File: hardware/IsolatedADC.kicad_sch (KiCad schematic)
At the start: 21 parts, among them IC3 OPA1679-Q1, IC4 ADS131M04, IC5 LTC1799, J6 CDMM20M0F2500DET, J9 CDMM20M0F2500DET

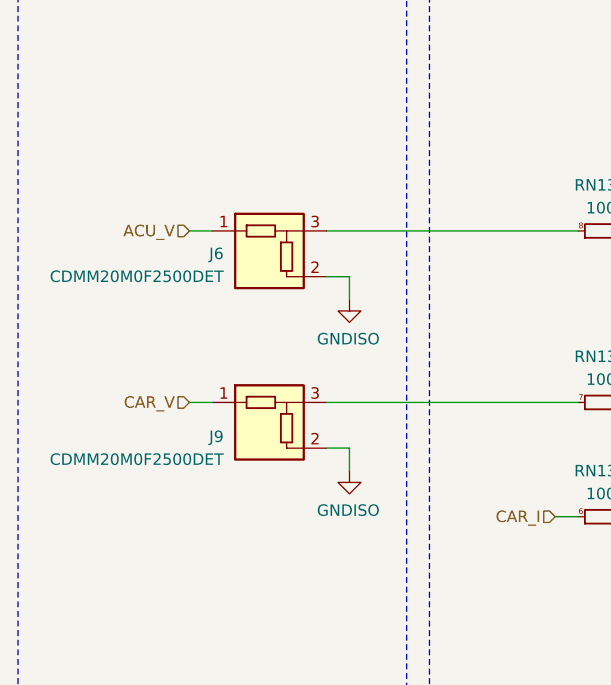
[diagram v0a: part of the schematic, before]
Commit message: new firmware for bga version of stm, change stm from smt to bga, smaller HV dividers, added 3rd can transciver, and other
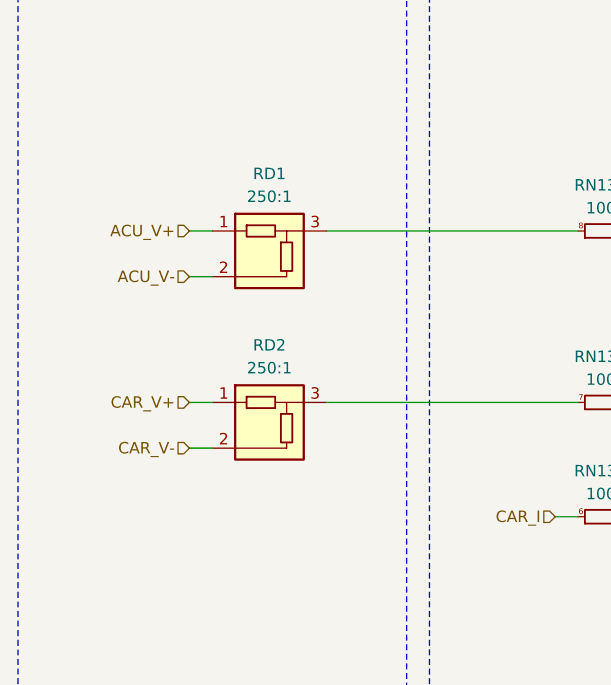
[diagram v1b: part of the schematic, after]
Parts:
- removed J6, J9: CDMM20M0F2500DET, Samacsys:CDMM20M0F2500DET, symbol Samacsys_kicad_sym:CDMM20M0F2500DET
- added RD1, RD2: 250:1, Samacsys:CDMA5M00F5000DE5, symbol Samacsys_kicad_sym:CDMA15M0D2500DE5
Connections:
- net at RN13.7 (R2.2): now also RD2.3
- net at RN13.8 (R1.2): now also RD1.3
- new net ACU_V+: RD1.1
- new net ACU_V-: RD1.2
- new net CAR_V+: RD2.1
- new net CAR_V-: RD2.2

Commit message: mama comit
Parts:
- removed C30: 10nF, Capacitor_SMD:C_0603_1608Metric, symbol Device:C_Small
- removed R1, R2, R3: 0, Resistor_SMD:R_0603_1608Metric, symbol Device:R_Small
- added R10: 10k, Resistor_SMD:R_0603_1608Metric, symbol Device:R_Small
- added R9: 100k, Resistor_SMD:R_0603_1608Metric, symbol Device:R_Small
- R15: value 10k -> 100k
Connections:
- net ACU_V- is gone; now on net GNDISO: RD1.2
- net CAR_V- is gone; now on net GNDISO: RD2.2
- net CAR_I_REF_ADC: no longer D4.1 (A), RN13.4 (R4.1)
- net GNDISO: now also R10.2
- net at IC3.11 (+): now also R10.1, R9.2
- new net: D4.1 (A), R9.1, RN13.4 (R4.1)
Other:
- moved on the sheet: D4, IC3A, IC3B, IC3C, IC3D, R15, R17, RD1, RD2, RN13A, RN13B, RN13C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

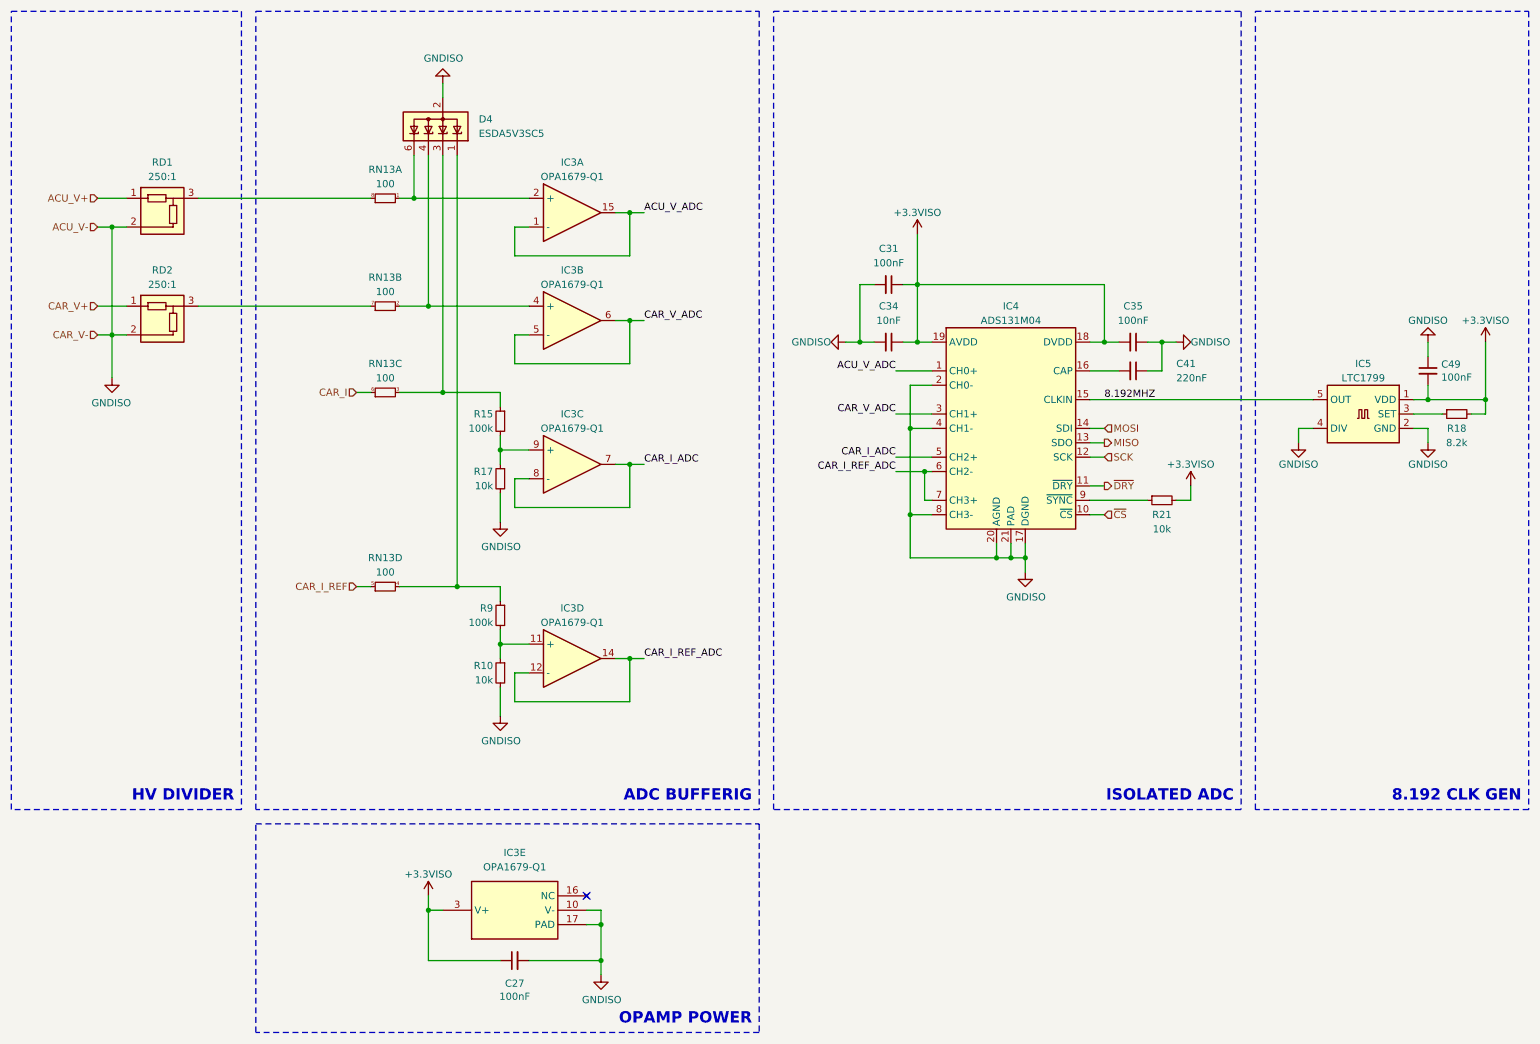
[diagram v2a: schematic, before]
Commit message: inductors 3d models fix, smaller relay (same series as the one from IMD), other + sync
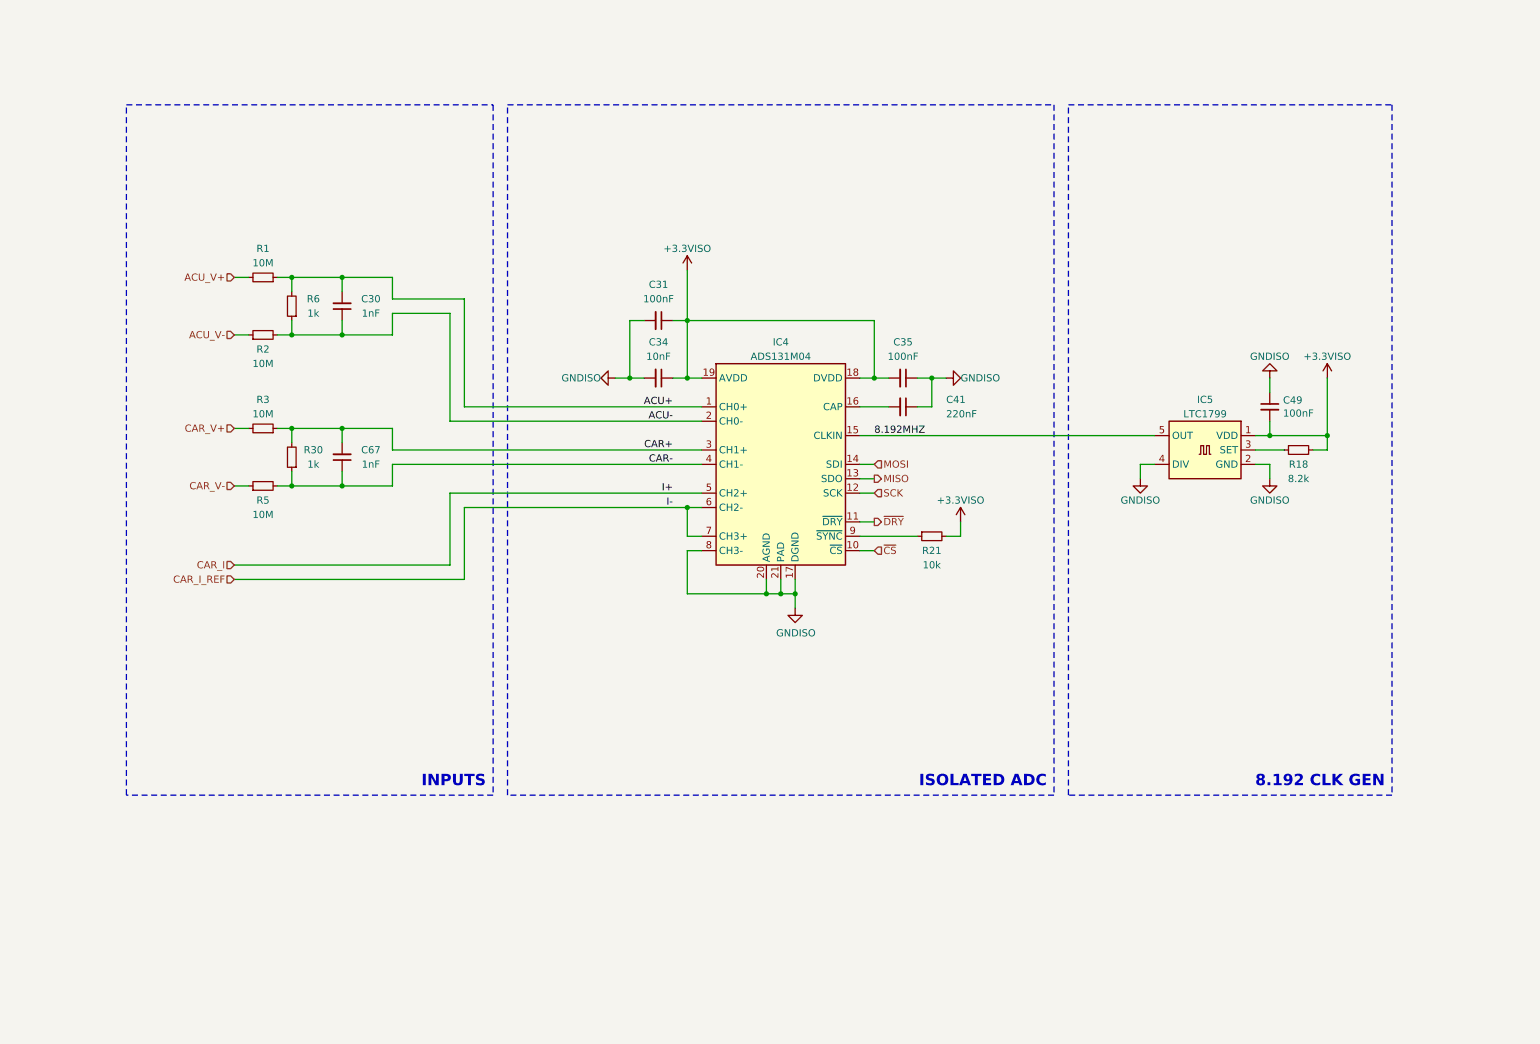
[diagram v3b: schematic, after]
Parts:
- removed C27: 100nF, Capacitor_SMD:C_0603_1608Metric, symbol Device:C_Small
- removed D4: ESDA5V3SC5, Package_TO_SOT_SMD:SOT-23-6, symbol Power_Protection:ESDA5V3SC5
- removed IC3: OPA1679-Q1, Package_DFN_QFN:QFN-16-1EP_4x4mm_P0.65mm_EP2.7x2.7mm, symbol Samacsys_kicad_sym:OPA1679-Q1
- removed R10, R17: 10k, Resistor_SMD:R_0603_1608Metric, symbol Device:R_Small
- removed R15, R9: 100k, Resistor_SMD:R_0603_1608Metric, symbol Device:R_Small
- removed RD1, RD2: 250:1, Samacsys:CDMA5M00F5000DE5, symbol Samacsys_kicad_sym:CDMA15M0D2500DE5
- removed RN13: 100, Resistor_SMD:R_Array_Convex_4x0603, symbol Device:R_Pack04_Split
- added C30, C67: 1nF, Capacitor_SMD:C_0603_1608Metric, symbol Device:C_Small
- added R1, R2, R3, R5: 10M, Resistor_SMD:R_0603_1608Metric, symbol Device:R_Small
- added R30, R6: 1k, Resistor_SMD:R_0603_1608Metric, symbol Device:R_Small
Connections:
- net CAR_I_ADC is gone; now on net CAR_I: IC4.5 (CH2+)
- net CAR_I_REF_ADC is gone; now on net CAR_I_REF: IC4.6 (CH2-), IC4.7 (CH3+)
- net ACU_V+: now also R1.2
- net CAR_V+: now also R3.2
- net GNDISO: no longer IC4.2 (CH0-), IC4.4 (CH1-)
- net ACU_V_ADC renamed ACU+
- net ACU+: now also C30.2, R1.1, R6.2
- net CAR_V_ADC renamed CAR+
- net CAR+: now also C67.2, R3.1, R30.2
- new net ACU-: C30.1, IC4.2 (CH0-), R2.2, R6.1
- new net ACU_V-: R2.1
- new net CAR-: C67.1, IC4.4 (CH1-), R30.1, R5.2
- new net CAR_V-: R5.1
- no-connect marks 1 -> 0
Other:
- note added: "INPUTS"
- note removed: "ADC BUFFERIG"
- note removed: "HV DIVIDER"
- note removed: "OPAMP POWER"
- moved on the sheet: C31, C34, C35, C41, C49, IC4, IC5, R18, R21

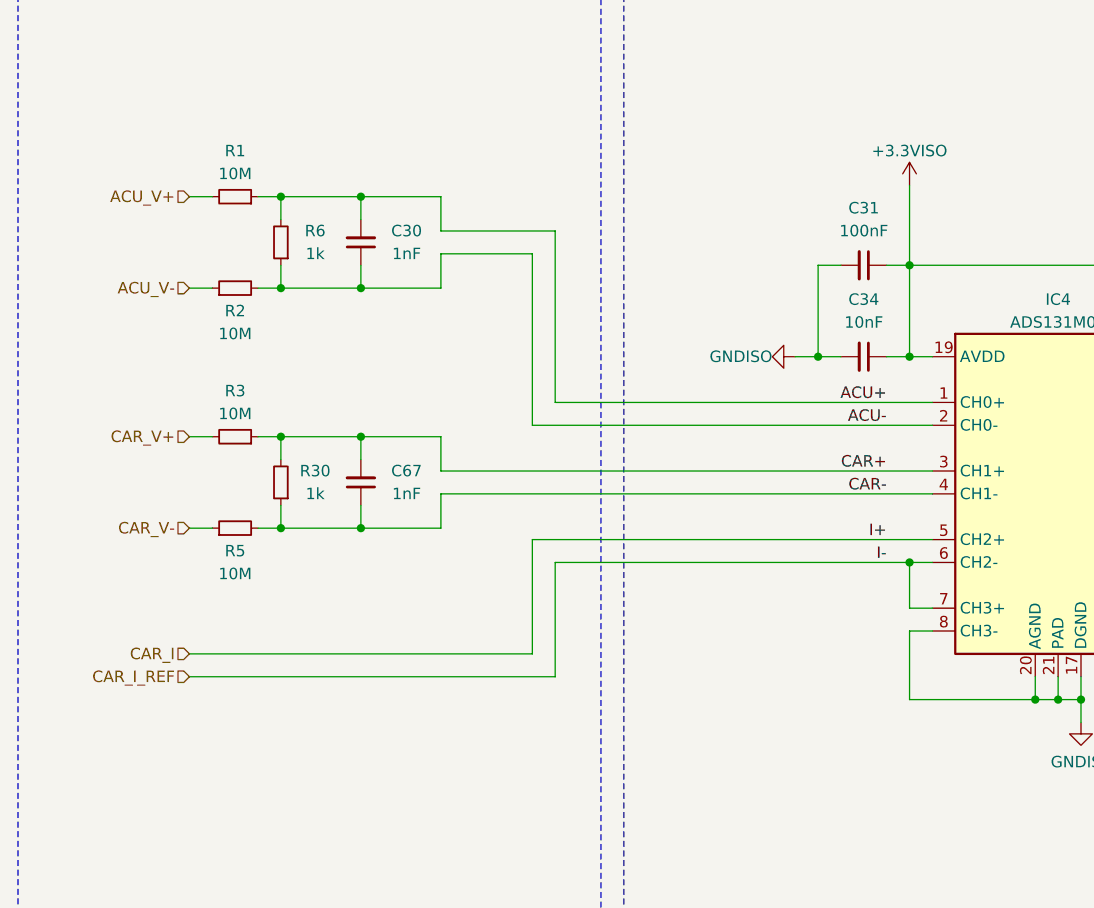
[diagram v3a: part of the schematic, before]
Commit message: all but the communications sections done
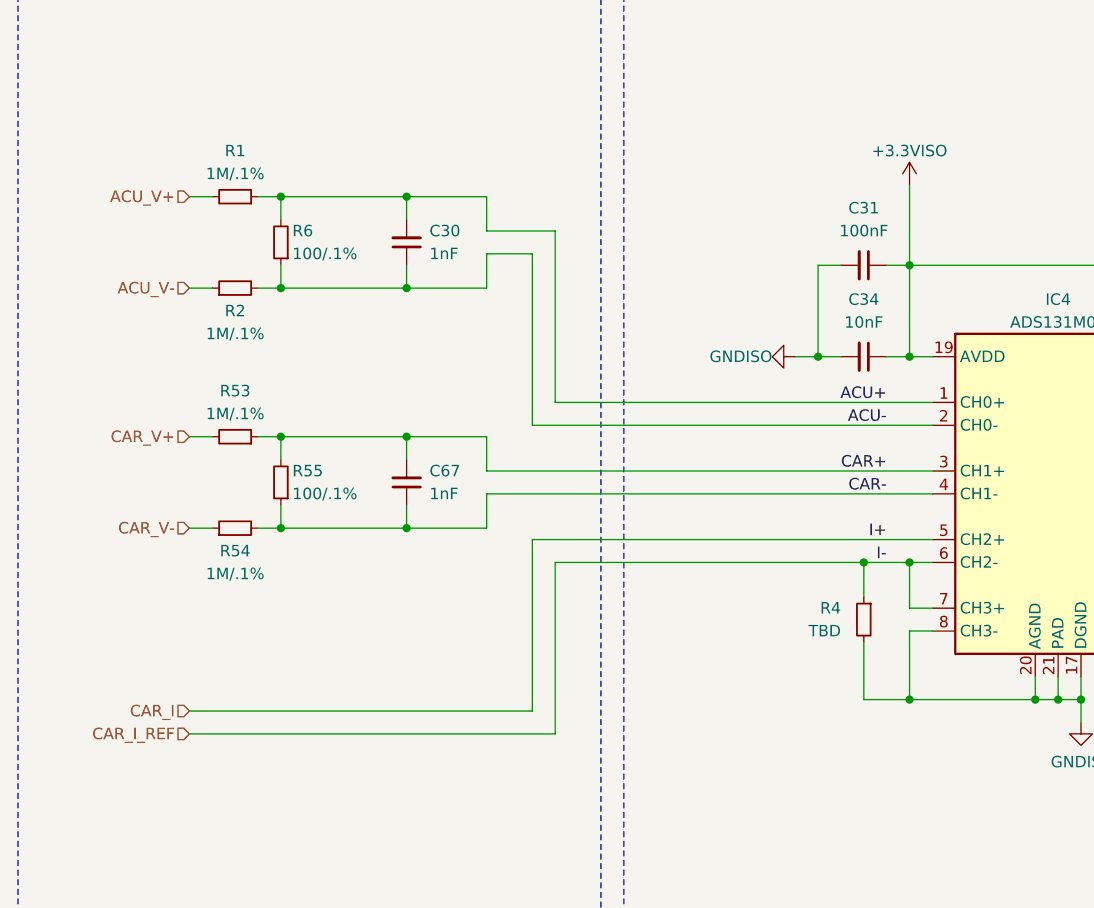
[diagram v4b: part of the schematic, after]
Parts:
- removed R3, R5: 10M, Resistor_SMD:R_0603_1608Metric, symbol Device:R_Small
- removed R30: 1k, Resistor_SMD:R_0603_1608Metric, symbol Device:R_Small
- added R4: TBD, Resistor_SMD:R_0603_1608Metric, symbol Device:R_Small
- added R53, R54: 1M/.1%, Resistor_SMD:R_1206_3216Metric, symbol Device:R_Small
- added R55: 100/.1%, Resistor_SMD:R_1206_3216Metric, symbol Device:R_Small
- R1, R2: value 10M -> 1M/.1%; footprint Resistor_SMD:R_0603_1608Metric -> Resistor_SMD:R_1206_3216Metric; Manufacturer_Name -- -> (none); Manufacturer_Part_Number -- -> 754-RGV3216P-1004BT1; Mouser Url (none) -> https://www.mouser.pl/ProductDetail/Susumu/RGV3216P-1004-B-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
- R6: value 1k -> 100/.1%; footprint Resistor_SMD:R_0603_1608Metric -> Resistor_SMD:R_1206_3216Metric
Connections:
- net CAR+: now also R53.1, R55.2
- net CAR-: now also R54.2, R55.1
- net CAR_I_REF: now also R4.1
- net CAR_V+: now also R53.2
- net CAR_V-: now also R54.1
- net GNDISO: now also R4.2
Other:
- moved on the sheet: C30, C67

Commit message: sync
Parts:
- added R93: 10k, Resistor_SMD:R_0603_1608Metric, symbol Device:R_Small
- R4: value TBD -> 10k
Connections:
- net +3.3VISO: now also R93.1
- net MISO: now also R93.2
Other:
- note added: "SPI PULLUP"
- moved on the sheet: C30, C31, C34, C35, C41, C49, C67, IC4, IC5, R1, R18, R2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

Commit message: sync
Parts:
- C31, C35, C49: Mouser Price/Stock (none) -> https://www.mouser.pl/ProductDetail/KEMET/C0603C104J3RACTU?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
- IC4: value ADS131M04 -> ~; Mouser Part Number (none) -> ADS131M04IRUKR; Mouser Price/Stock (none) -> https://www.mouser.pl/ProductDetail/Texas-Instruments/ADS13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
- R1, R2, R53, R54: Mouser Price/Stock (none) -> https://www.mouser.pl/ProductDetail/Susumu/RGV3216P-1004-B-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; Mouser Url https://www.mouser.pl/ProductDetail/Susumu/RGV3216P-1004-B-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 -> (none)
- R21, R4, R93: Mouser Price/Stock (none) -> https://www.mouser.pl/ProductDetail/YAGEO/RT0603DRE07100KL?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

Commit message: layotu done, some more routing done
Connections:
- net CAP: now reaches C41.2, IC4.16 (CAP)
- net SET: now reaches IC5.3 (SET), R18.1
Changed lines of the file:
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@@
+		)
+	)
+	(label "CAP"
+		(at 156.21 85.09 0)
+		(fields_autoplaced yes)
+		(effects
+			(font
+				(size 0.5 0.5)
+			)
+			(justify left bottom)
 		)
 	)
@@
 		)
 	)
+	(label "SET"
+		(at 250.19 92.71 0)
+		(fields_autoplaced yes)
+		(effects
+			(font
+				(size 0.5 0.5)
+			)
+			(justify left bottom)
+		)
+	)

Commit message: sync
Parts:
- R1, R2, R53, R54: value 1M/.1% -> 1M/700V/.1%
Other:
- moved on the sheet: R1, R2, R53, R54, R55, R6
